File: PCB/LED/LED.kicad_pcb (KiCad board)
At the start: 2 copper layers, 70 x 70 mm, 24 parts, among them J1 Conn_01x03, J3 Shelly, J4 USB-PROG, J5 USB-C-Socket-H, U6 ESP32-S3-MINI-1, U7 MD8942

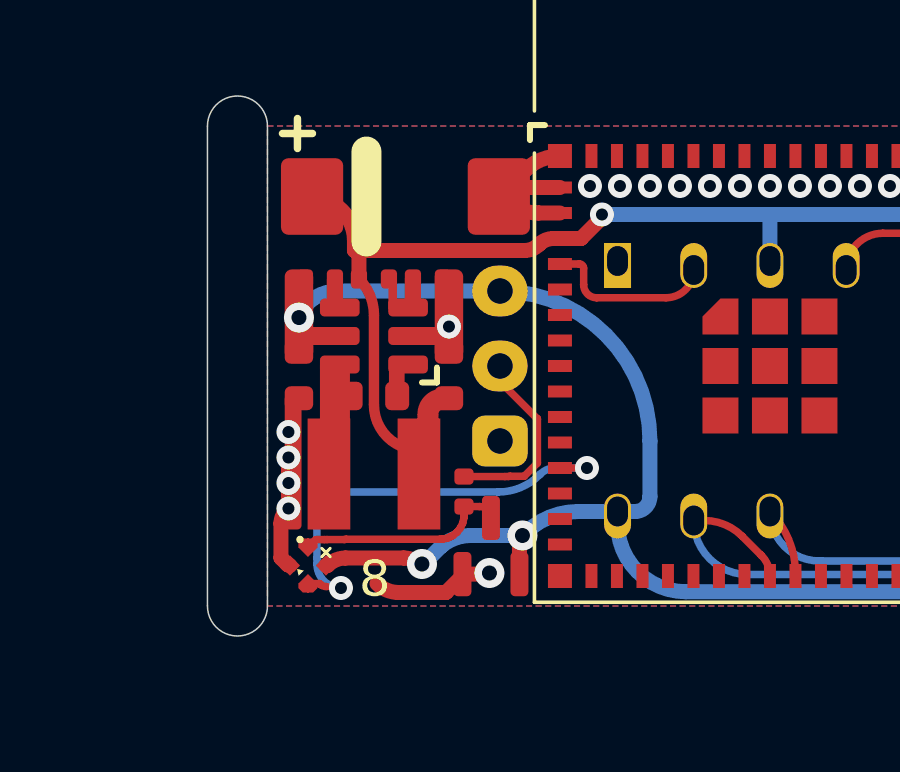
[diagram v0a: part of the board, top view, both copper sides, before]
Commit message: Solder tabs
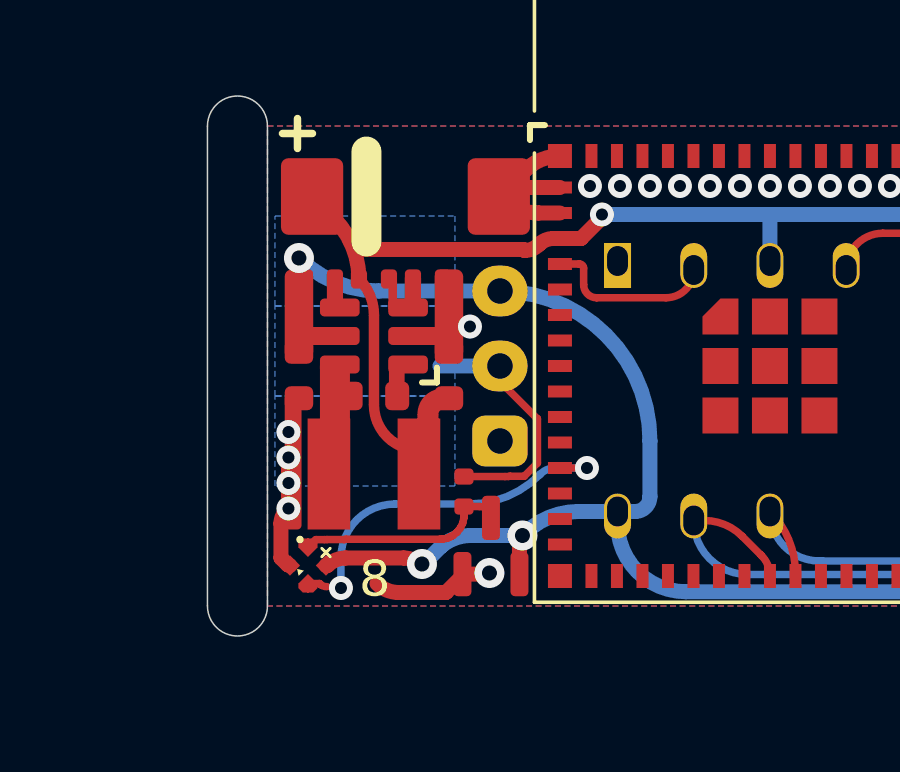
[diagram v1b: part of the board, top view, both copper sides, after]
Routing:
- net LED: track 14.0 -> 12.0 mm
- net Net-(J1-Pin_2): track 6.34 -> 7.65 mm
- net DC: track 63.8 -> 65.0 mm
- net +3V3: track 35.3 -> 34.1 mm
- net GND: track 18.8 -> 17.7 mm
- added copper zone on B.Cu, net DC
- added copper zone on B.Cu, net Net-(J1-Pin_2)
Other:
- board text removed: "LED:8"

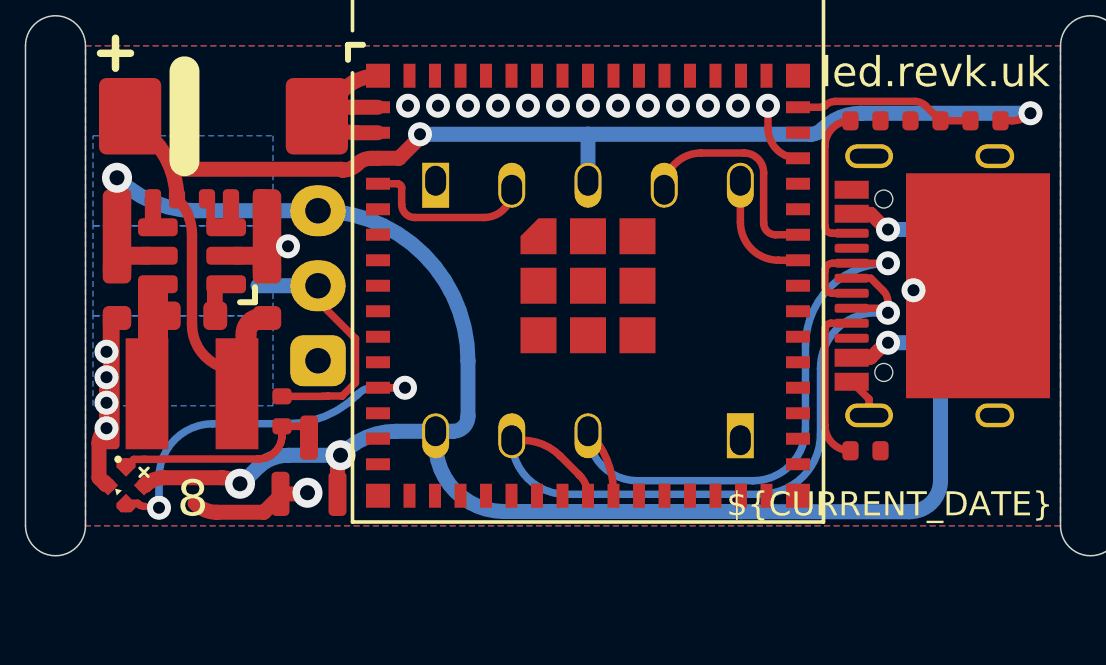
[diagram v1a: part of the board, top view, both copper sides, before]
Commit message: Revised for new placement of the USB-C FFS
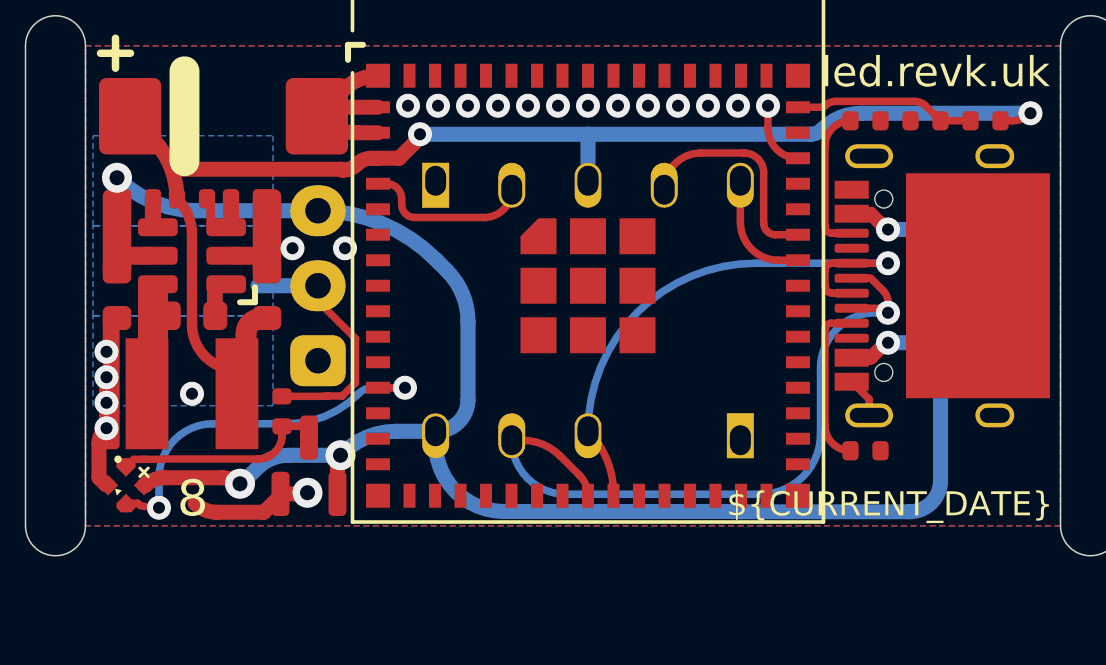
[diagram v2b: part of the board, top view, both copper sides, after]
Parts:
- moved J5 2.22 mm to (108.8, 102.0)
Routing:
- net D+: track 22.0 -> 19.0 mm
- net GND: vias 20 -> 21

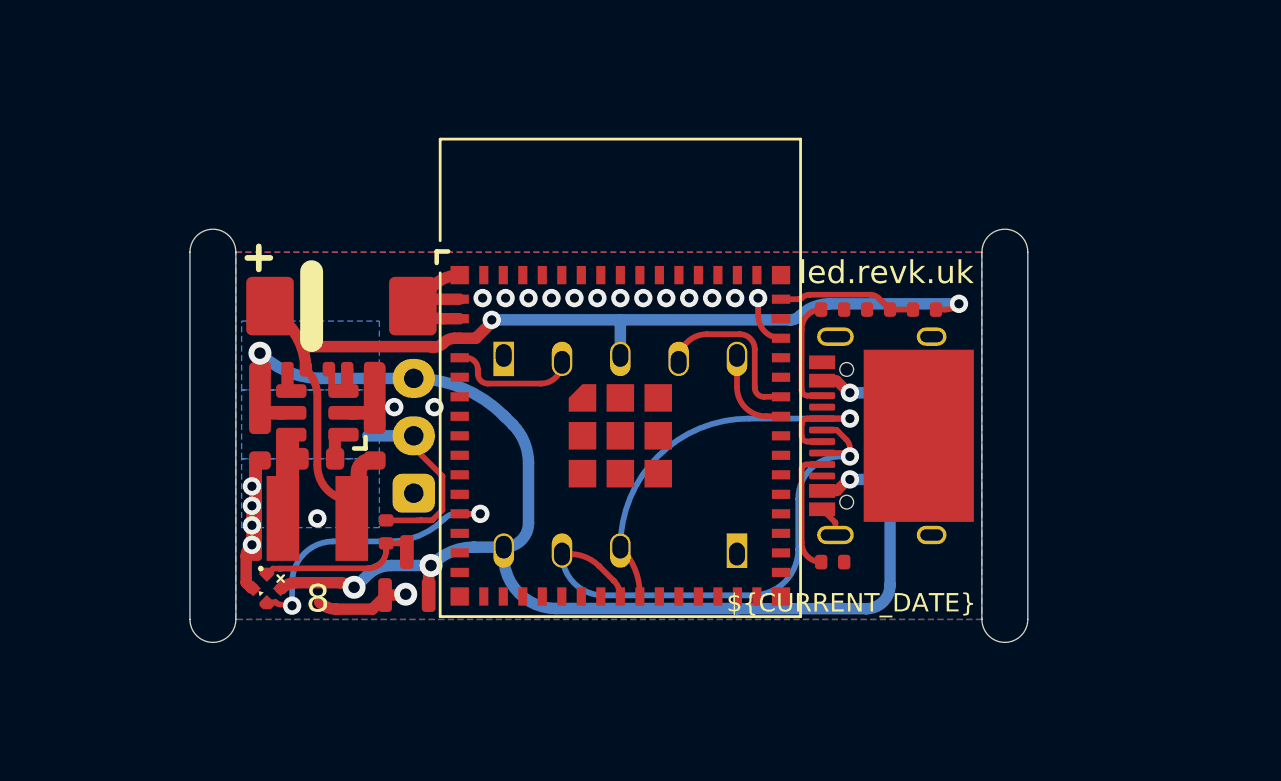
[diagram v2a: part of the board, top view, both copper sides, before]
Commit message: Allow screw terminal
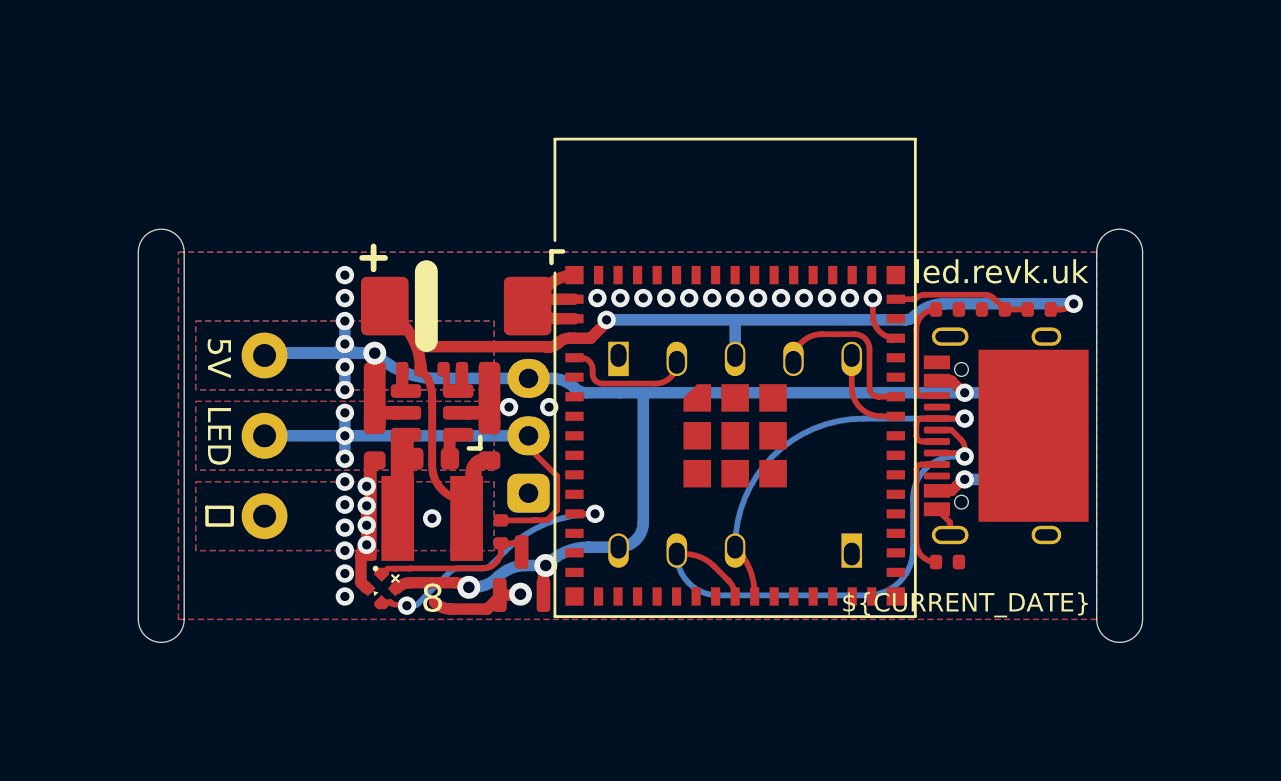
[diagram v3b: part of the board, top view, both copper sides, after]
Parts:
- added J2: Conn_01x03, RevK:MP011985, F.Cu at (84.2, 102.0)
- moved C1 5.00 mm to (92.6, 96.3)
- moved C10 5.00 mm to (89.0, 102.3)
- moved C11 5.00 mm to (94.0, 102.3)
- moved C12 5.00 mm to (91.5, 103.0)
- moved C9 5.00 mm to (116.0, 96.5)
- moved D1 5.00 mm to (89.3, 108.7)
- moved D3 5.00 mm to (95.5, 108.0)
- moved J1 5.00 mm to (95.8, 102.0)
- moved J3 5.00 mm to (104.8, 98.7)
- moved J4 5.00 mm to (104.8, 107.0)
- moved J5 5.00 mm to (113.8, 102.0)
- moved L2 5.00 mm to (91.5, 105.6)
- moved R14 5.00 mm to (93.4, 99.1)
- moved R15 5.00 mm to (89.8, 99.1)
- moved R2 5.00 mm to (118.0, 96.5)
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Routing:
- net Net-(J1-Pin_2): track 7.65 -> 19.2 mm, vias 0 -> 3
- net DC: track 65.1 -> 69.4 mm, vias 5 -> 9
- net LED: track 12.0 -> 11.1 mm
- net GND: vias 21 -> 29
- added copper zone on F.Cu, net DC
- added copper zone on F.Cu, net Net-(J1-Pin_2)

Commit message: Lots of buggering about to get aligned
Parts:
- moved J5 0.83 mm to (114.6, 102.0)
- turned J2 to -90 degrees
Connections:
- J2 pad 1: GND -> DC
- J2 pad 3: DC -> GND

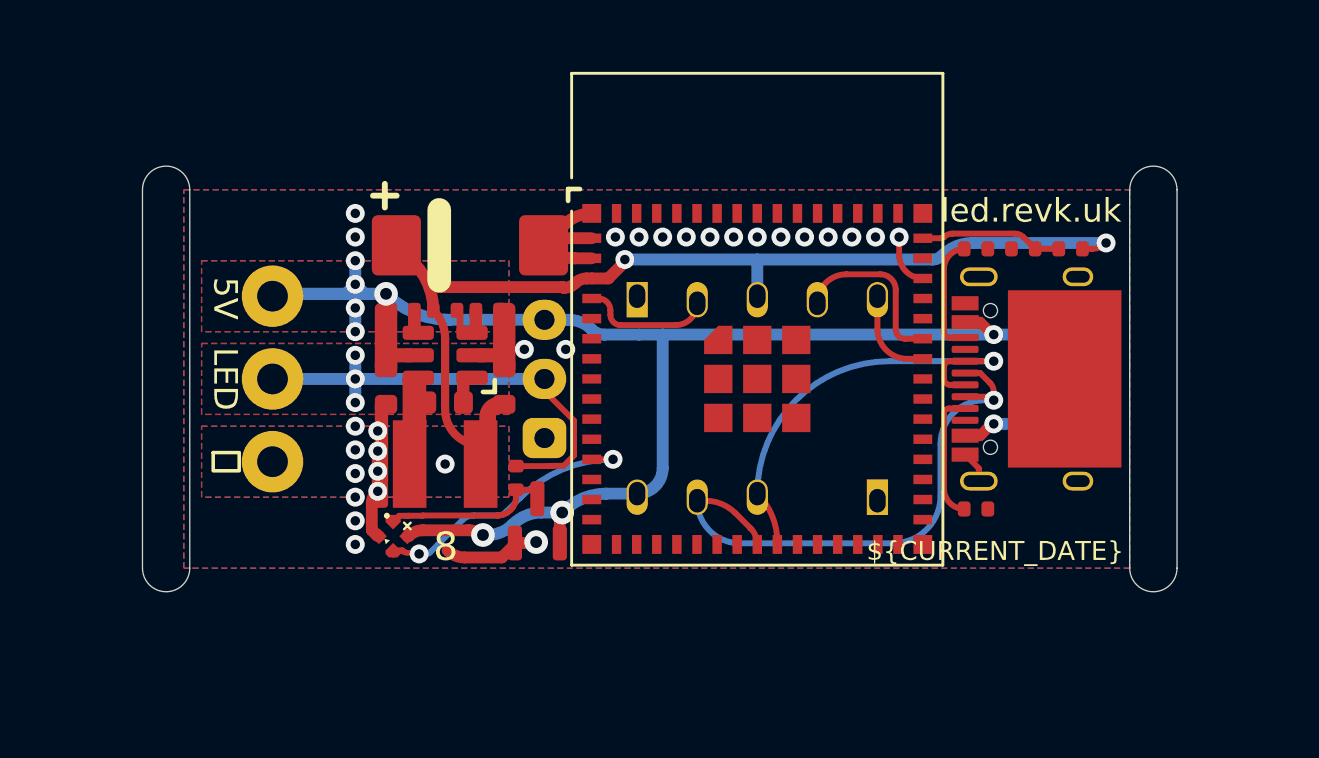
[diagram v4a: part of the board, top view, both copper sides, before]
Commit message: Round corners
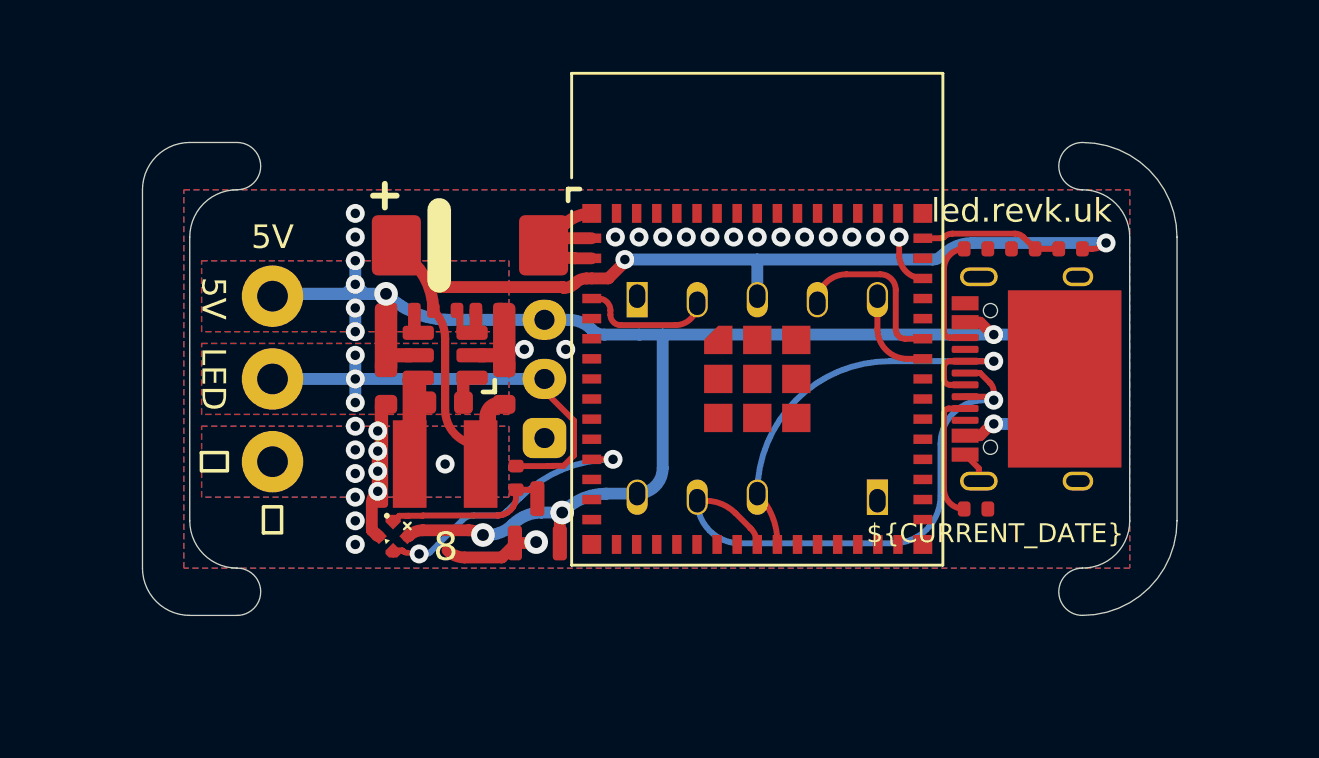
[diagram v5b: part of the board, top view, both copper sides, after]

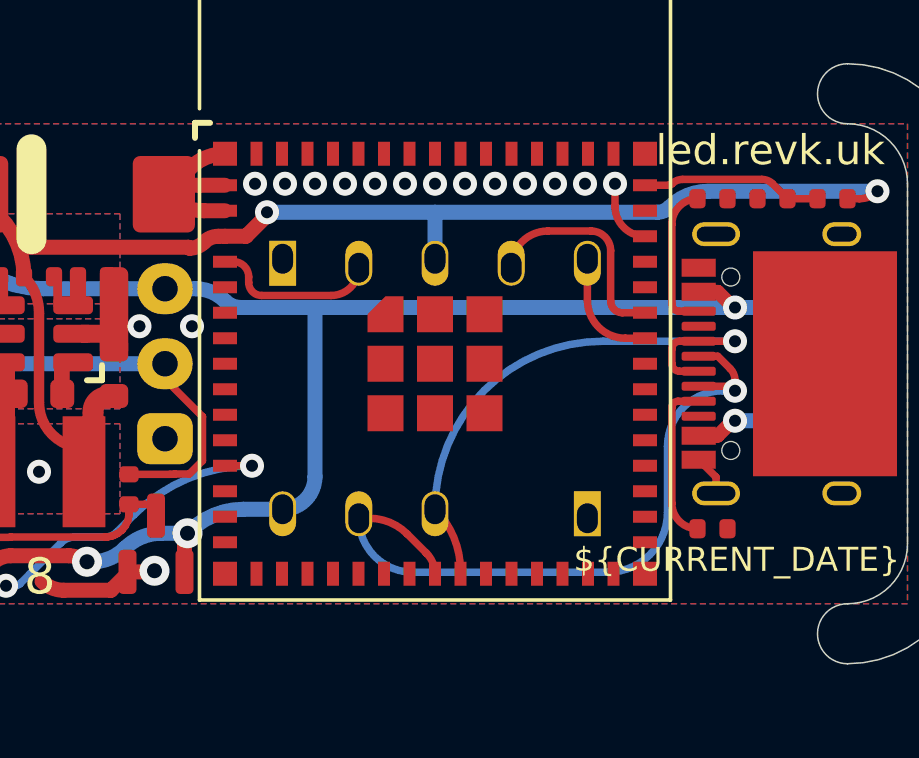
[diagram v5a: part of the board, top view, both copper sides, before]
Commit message: Change USB connector on back of processor
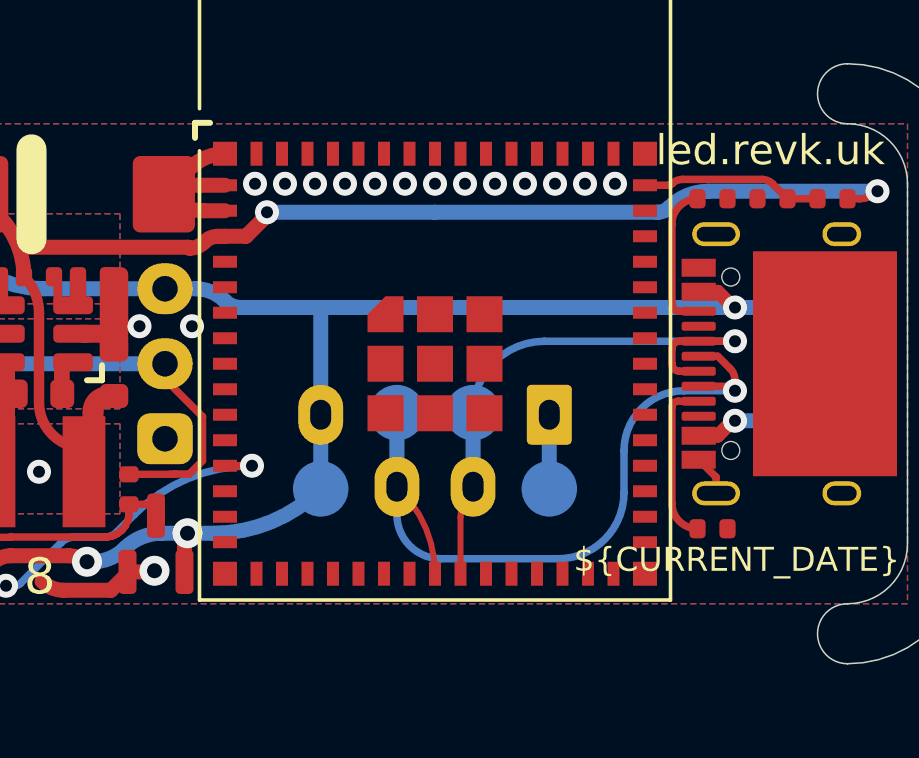
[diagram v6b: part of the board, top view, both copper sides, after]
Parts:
- removed J3: Shelly, RevK:Shelly
- J4: footprint RevK:USB-PROG -> RevK:USB-PROG2
- moved J4 2.10 mm to (104.8, 104.9)
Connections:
- U6 pad 39: Net-(J3-Tx) -> unconnected-(U6-GPIO43-Pad39)
- U6 pad 4: Net-(J3-0) -> unconnected-(U6-GPIO0-Pad4)
- U6 pad 40: Net-(J3-Rx) -> unconnected-(U6-GPIO44-Pad40)
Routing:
- net Net-(J3-Rx): track 7.34 -> 0.00 mm
- net Net-(J3-0): track 5.64 -> 0.00 mm
- net Net-(J3-Tx): track 3.97 -> 0.00 mm
- net +3V3: track 34.1 -> 32.6 mm
- net D-: track 24.4 -> 25.6 mm

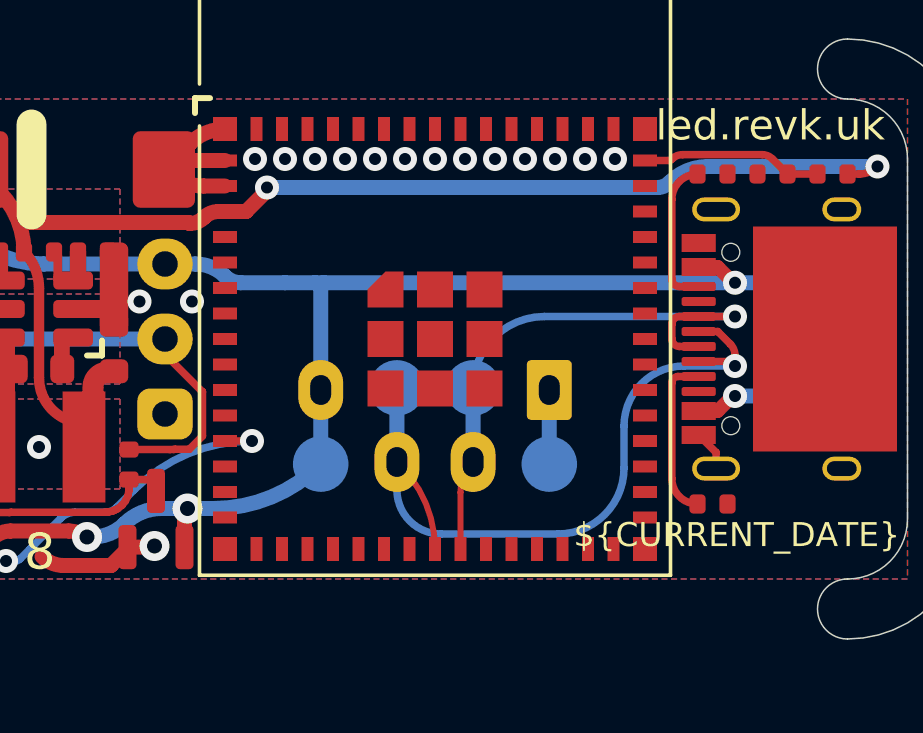
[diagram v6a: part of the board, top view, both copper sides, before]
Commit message: Remove USB on back of CPU
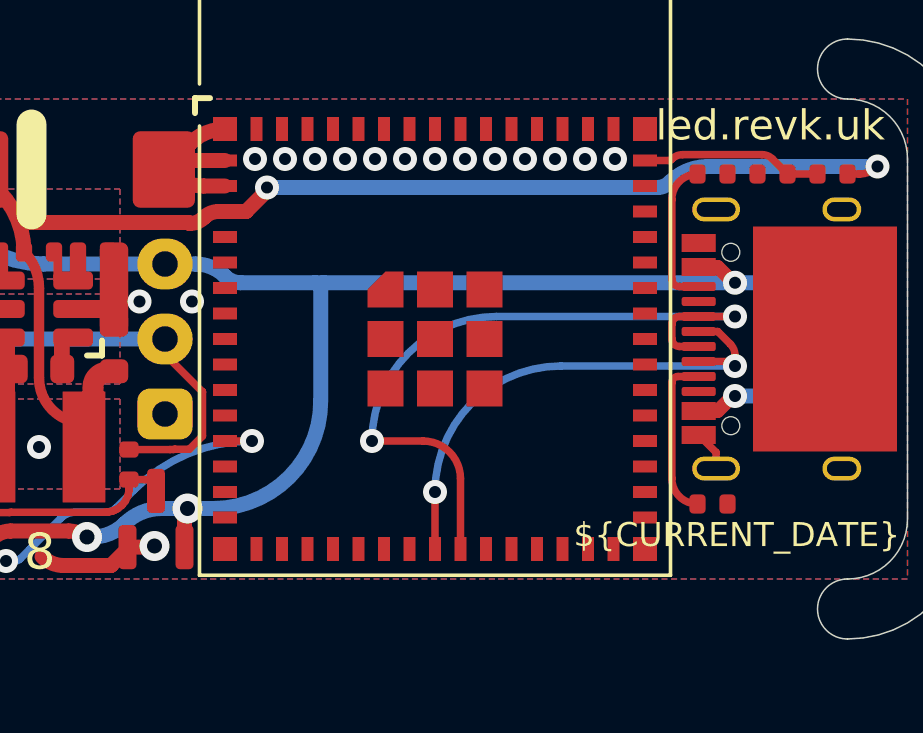
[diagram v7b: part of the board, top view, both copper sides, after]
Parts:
- removed J4: USB-PROG, RevK:USB-PROG2
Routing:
- net D-: track 25.6 -> 17.4 mm, vias 1 -> 2
- net D+: track 19.2 -> 24.0 mm, vias 1 -> 2
- net GND: track 17.9 -> 15.4 mm
- net DC: track 69.7 -> 69.1 mm
